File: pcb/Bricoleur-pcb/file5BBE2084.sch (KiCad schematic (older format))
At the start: 4 parts

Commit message: Schematics and footprints almost done
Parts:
- added C14, C15, C16: 1N, Capacitor_SMD:C_0402_1005Metric, symbol Device:C
- added D1, D2, D3: LED, LED_SMD:LED_0201_0603Metric, symbol Device:LED
- added R10, R9: 3K, Capacitor_SMD:C_0402_1005Metric, symbol Device:R
- added R11, R12, R13: 100R, Resistor_SMD:R_0402_1005Metric, symbol Device:R
- added R17: 100K, Resistor_SMD:R_0402_1005Metric, symbol Device:R
- added R5, R6, R7: 1M, Resistor_SMD:R_0402_1005Metric, symbol Device:R
- added R8: 3K, Resistor_SMD:R_0402_1005Metric, symbol Device:R
- added SW3, SW4, SW5: SW_Push, Bricoleur-custom:SWITCH_WURTH_4301182043816, symbol Switch:SW_Push
- added U10: VESD05A8A-HNH, Bricoleur-custom:VESD05A8A-HNH, symbol Bricoleur-pcb-cache:VESD05A8A-HNH
- J2: renamed from J?; footprint (none) -> Connector_PinHeader_2.54mm:PinHeader_2x10_P2.54mm_Vertical
- R14, R15: renamed from R?; footprint (none) -> Resistor_SMD:R_0402_1005Metric
- R16: renamed from R?; value R -> 10K; footprint (none) -> Resistor_SMD:R_0402_1005Metric
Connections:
- net labels added: DBG_LED_1, DBG_LED_2, DBG_LED_3, DBG_PB_1, DBG_PB_2, DBG_PB_3
- net labels removed: DH_RTCK
- wire segments 24 -> 90
- no-connect marks 0 -> 1

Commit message: Start of layout work + minor tweaks
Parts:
- J2: footprint Connector_PinHeader_2.54mm:PinHeader_2x10_P2.54mm_Vertical -> Connector_IDC:IDC-Header_2x10_P2.54mm_Vertical
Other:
- note removed: "UNFINISHED\n"
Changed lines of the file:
@@
 F 0 "J2" H 9100 2717 50  0000 C CNN
 F 1 "Conn_02x10_Odd_Even" H 9100 2626 50  0000 C CNN
-F 2 "Connector_PinHeader_2.54mm:PinHeader_2x10_P2.54mm_Vertical" H 9050 2100 50  0001 C CNN
+F 2 "Connector_IDC:IDC-Header_2x10_P2.54mm_Vertical" H 9050 2100 50  0001 C CNN
 F 3 "~" H 9050 2100 50  0001 C CNN
 	1    9050 2100
@@
 Text GLabel 9950 2500 3    50   Input ~ 0
 DEBUG_EXT_CABLE_ATTACH
-Text Notes 10400 2150 1    50   ~ 0
-UNFINISHED\n
 $Comp
 L Device:LED D1

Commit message: Finished camera connection, started on MC. Changed debug protection diodes sharing pattern to match debug connector.
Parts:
- U10: symbol Bricoleur-pcb-cache:VESD05A8A-HNH -> Bricoleur-pcb-rescue:VESD05A8A-HNH-Bricoleur-pcb-cache
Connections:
- wire segments 90 -> 84
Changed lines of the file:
@@
 Text GLabel 9500 2900 3    50   Input ~ 0
 GND
-Wire Wire Line
-	9350 2500 9850 2500
 Text GLabel 9950 1650 1    50   Input ~ 0
 PYNQ_3V3
@@
 Wire Wire Line
 	4700 1550 5200 1550
-Connection ~ 5200 1550
-Wire Wire Line
-	5200 1550 5500 1550
-Connection ~ 5500 1550
 Wire Wire Line
 	5500 1550 5750 1550
@@
 Wire Wire Line
 	4700 1800 4700 1750
-Connection ~ 5200 1800
 Wire Wire Line
 	5200 1800 4700 1800
-Connection ~ 5500 1800
-Wire Wire Line
-	5500 1800 5200 1800
 Wire Wire Line
 	5750 2100 5500 2100
 Wire Wire Line
 	4700 2100 4700 2050
-Connection ~ 5200 2100
 Wire Wire Line
 	5200 2100 4700 2100
-Connection ~ 5500 2100
-Wire Wire Line
-	5500 2100 5200 2100
 Wire Wire Line
 	6050 1550 6200 1550
@@
 	5150 4550 5150 4450
 $Comp
-L Bricoleur-pcb-cache:VESD05A8A-HNH U10
+L Bricoleur-pcb-rescue:VESD05A8A-HNH-Bricoleur-pcb-cache U10
 U 1 1 5BA605D7
 P 8300 1550
@@
 $EndComp
 Wire Wire Line
-	8750 1300 8750 1400
-Wire Wire Line
-	8750 1400 9850 1400
-Wire Wire Line
-	9850 1400 9850 2500
-Connection ~ 9850 2500
-Wire Wire Line
-	9850 2500 9950 2500
-Wire Wire Line
-	8850 1700 8650 1700
-Wire Wire Line
-	8850 1800 8550 1800
-Wire Wire Line
-	8850 1900 8450 1900
-Wire Wire Line
-	8850 2000 8350 2000
-Wire Wire Line
-	8850 2100 8250 2100
-Wire Wire Line
-	8850 2400 8050 2400
-Wire Wire Line
-	8650 1300 8650 1700
-Connection ~ 8650 1700
-Wire Wire Line
-	8650 1700 7850 1700
-Wire Wire Line
-	8550 1300 8550 1800
-Connection ~ 8550 1800
-Wire Wire Line
-	8550 1800 7850 1800
-Wire Wire Line
-	8450 1300 8450 1900
-Connection ~ 8450 1900
-Wire Wire Line
-	8450 1900 7850 1900
-Wire Wire Line
-	8350 1300 8350 2000
-Connection ~ 8350 2000
-Wire Wire Line
-	8350 2000 7850 2000
-Wire Wire Line
-	8250 1300 8250 2100
-Connection ~ 8250 2100
-Wire Wire Line
-	8250 2100 7850 2100
-Wire Wire Line
 	7100 2200 8850 2200
-Wire Wire Line
-	7850 2300 8150 2300
-Wire Wire Line
-	8150 1300 8150 2300
-Connection ~ 8150 2300
-Wire Wire Line
-	8150 2300 8850 2300
-Wire Wire Line
-	8050 1300 8050 2400
-Connection ~ 8050 2400
-Wire Wire Line
-	8050 2400 7850 2400
 Text GLabel 8050 750  2    50   Input ~ 0
 GND
@@
 VMCU
 NoConn ~ 9350 1700
+Wire Wire Line
+	9350 2500 9950 2500
+Text GLabel 8050 2450 3    50   Input ~ 0
+DEBUG_EXT_CABLE_ATTACH
+Wire Wire Line
+	7850 2100 8350 2100
+Wire Wire Line
+	7850 2300 8250 2300
+Wire Wire Line
+	7850 2400 8150 2400
+Wire Wire Line
+	7850 2000 8750 2000
+Wire Wire Line
+	7850 1900 8650 1900
+Wire Wire Line
+	7850 1700 8450 1700
+Wire Wire Line
+	7850 1800 8550 1800
+Wire Wire Line
+	8450 1300 8450 1700
+Connection ~ 8450 1700
+Wire Wire Line
+	8450 1700 8850 1700
+Wire Wire Line
+	8550 1300 8550 1800
+Connection ~ 8550 1800
+Wire Wire Line
+	8550 1800 8850 1800
+Wire Wire Line
+	8650 1300 8650 1900
+Connection ~ 8650 1900
+Wire Wire Line
+	8650 1900 8850 1900
+Wire Wire Line
+	8750 1300 8750 2000
+Connection ~ 8750 2000
+Wire Wire Line
+	8750 2000 8850 2000
+Wire Wire Line
+	8350 1300 8350 2100
+Connection ~ 8350 2100
+Wire Wire Line
+	8350 2100 8850 2100
+Wire Wire Line
+	8250 1300 8250 2300
+Connection ~ 8250 2300
+Wire Wire Line
+	8250 2300 8850 2300
+Wire Wire Line
+	8150 1300 8150 2400
+Connection ~ 8150 2400
+Wire Wire Line
+	8150 2400 8850 2400
+Wire Wire Line
+	8050 1300 8050 2450
 $EndSCHEMATC

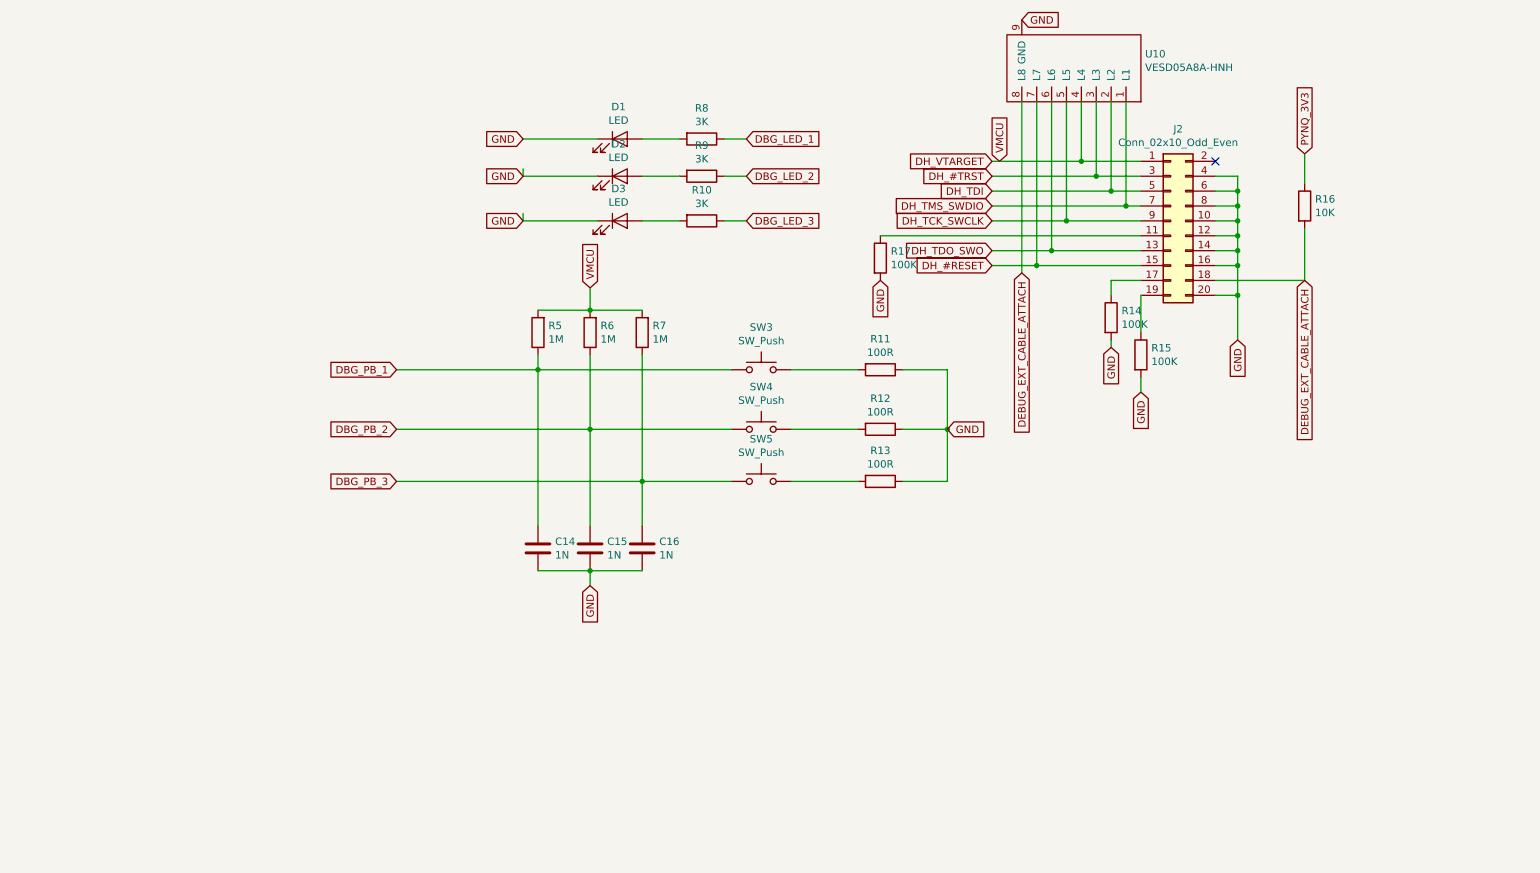
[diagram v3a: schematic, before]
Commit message: More ESD protection, USART output, more footprints
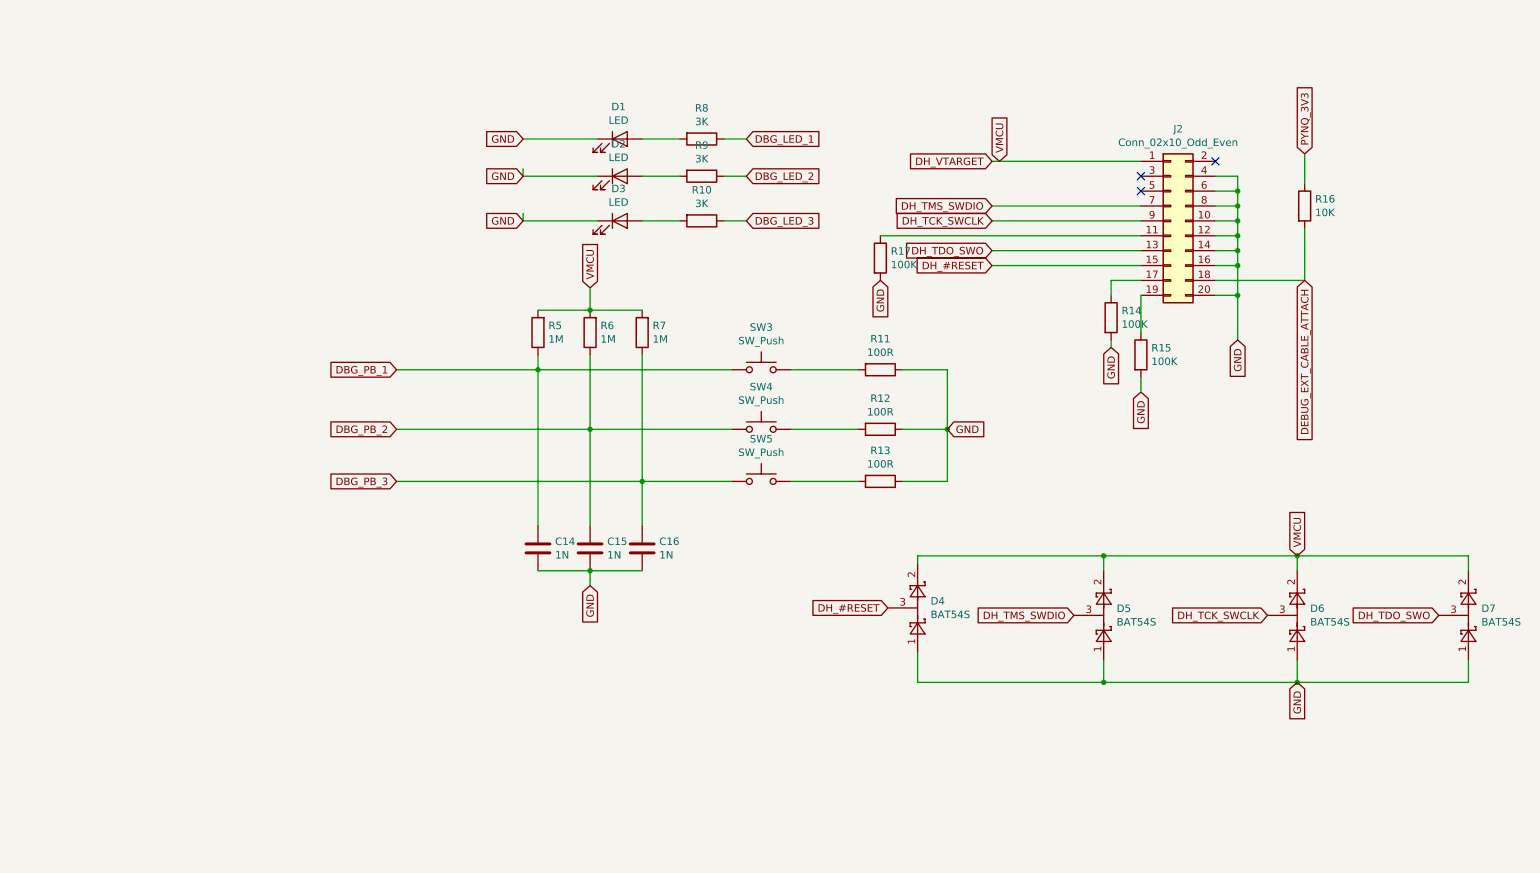
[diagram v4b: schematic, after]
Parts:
- removed U10: VESD05A8A-HNH, Bricoleur-custom:VESD05A8A-HNH, symbol Bricoleur-pcb-rescue:VESD05A8A-HNH-Bricoleur-pcb-cache
- added D4, D5, D6, D7: BAT54S, Package_TO_SOT_SMD:SOT-23, symbol Diode:BAT54S
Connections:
- net DH_#RESET: now also D4.3
- net DH_TCK_SWCLK: now also D6.3
- net DH_TDO_SWO: now also D7.3
- net DH_TMS_SWDIO: now also D5.3
- net DH_VTARGET: now also D4.2, D5.2, D6.2, D7.2
- net GND: now also D4.1, D5.1, D6.1, D7.1
- net DH_#TRST: no longer names the net of J2.3 (Pin_3)
- net DH_TDI: no longer names the net of J2.5 (Pin_5)
- no-connect marks 1 -> 3
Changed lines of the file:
@@
 $Descr A4 11693 8268
 encoding utf-8
-Sheet 2 3
+Sheet 2 18
 Title ""
 Date ""
@@
 Text GLabel 7850 1700 0    50   Input ~ 0
 DH_VTARGET
-Text GLabel 7850 1800 0    50   Input ~ 0
-DH_#TRST
-Text GLabel 7850 1900 0    50   Input ~ 0
-DH_TDI
 Text GLabel 7850 2000 0    50   Input ~ 0
 DH_TMS_SWDIO
@@
 DBG_PB_3
 Wire Wire Line
-	3850 3100 4800 3100
-Wire Wire Line
-	6100 3500 5150 3500
-Wire Wire Line
-	6100 3850 5500 3850
-Wire Wire Line
 	5150 2550 5150 2700
-Wire Wire Line
-	5500 2700 5150 2700
-Connection ~ 5150 2700
-Wire Wire Line
-	5150 2700 4800 2700
-Wire Wire Line
-	4800 3000 4800 3100
-Connection ~ 4800 3100
-Wire Wire Line
-	4800 3100 6100 3100
-Wire Wire Line
-	4800 3100 4800 4150
 Wire Wire Line
 	5150 3000 5150 3500
 Connection ~ 5150 3500
 Wire Wire Line
-	5150 3500 3850 3500
-Wire Wire Line
 	5150 3500 5150 4150
 Wire Wire Line
@@
 Connection ~ 5500 3850
 Wire Wire Line
-	5500 3850 3850 3850
-Wire Wire Line
 	5500 3850 5500 4150
 Wire Wire Line
@@
 GND
 Wire Wire Line
-	5500 4450 5150 4450
-Connection ~ 5150 4450
-Wire Wire Line
-	5150 4450 4800 4450
-Wire Wire Line
 	5150 4550 5150 4450
-$Comp
-L Bricoleur-pcb-rescue:VESD05A8A-HNH-Bricoleur-pcb-cache U10
-U 1 1 5BA605D7
-P 8300 1550
-F 0 "U10" H 7722 979 50  0000 R CNN
-F 1 "VESD05A8A-HNH" H 7722 1070 50  0000 R CNN
-F 2 "Bricoleur-custom:VESD05A8A-HNH" H 8300 1550 50  0001 C CNN
-F 3 "" H 8300 1550 50  0001 C CNN
-	1    8300 1550
-	-1   0    0    1
-$EndComp
 Wire Wire Line
 	7100 2200 8850 2200
-Text GLabel 8050 750  2    50   Input ~ 0
-GND
 $Comp
 L Device:R R17
@@
 Wire Wire Line
 	9350 2500 9950 2500
-Text GLabel 8050 2450 3    50   Input ~ 0
-DEBUG_EXT_CABLE_ATTACH
-Wire Wire Line
-	7850 2100 8350 2100
-Wire Wire Line
-	7850 2300 8250 2300
-Wire Wire Line
-	7850 2400 8150 2400
-Wire Wire Line
-	7850 2000 8750 2000
-Wire Wire Line
-	7850 1900 8650 1900
-Wire Wire Line
-	7850 1700 8450 1700
-Wire Wire Line
-	7850 1800 8550 1800
-Wire Wire Line
-	8450 1300 8450 1700
-Connection ~ 8450 1700
-Wire Wire Line
-	8450 1700 8850 1700
-Wire Wire Line
-	8550 1300 8550 1800
-Connection ~ 8550 1800
-Wire Wire Line
-	8550 1800 8850 1800
-Wire Wire Line
-	8650 1300 8650 1900
-Connection ~ 8650 1900
-Wire Wire Line
-	8650 1900 8850 1900
-Wire Wire Line
-	8750 1300 8750 2000
-Connection ~ 8750 2000
-Wire Wire Line
-	8750 2000 8850 2000
-Wire Wire Line
-	8350 1300 8350 2100
-Connection ~ 8350 2100
-Wire Wire Line
-	8350 2100 8850 2100
-Wire Wire Line
-	8250 1300 8250 2300
-Connection ~ 8250 2300
-Wire Wire Line
-	8250 2300 8850 2300
-Wire Wire Line
-	8150 1300 8150 2400
-Connection ~ 8150 2400
-Wire Wire Line
-	8150 2400 8850 2400
-Wire Wire Line
-	8050 1300 8050 2450
+Wire Wire Line
+	3850 3100 4800 3100
+Wire Wire Line
+	4800 3100 4800 4150
+Wire Wire Line
+	4800 3000 4800 3100
+Connection ~ 4800 3100
+Wire Wire Line
+	4800 3100 6100 3100
+Wire Wire Line
+	6100 3500 5150 3500
+Wire Wire Line
+	6100 3850 5500 3850
+Connection ~ 5150 2700
+Wire Wire Line
+	5500 2700 5150 2700
+Wire Wire Line
+	5150 2700 4800 2700
+Connection ~ 5150 4450
+Wire Wire Line
+	5500 4450 5150 4450
+Wire Wire Line
+	5150 4450 4800 4450
+Wire Wire Line
+	5150 3500 3850 3500
+Wire Wire Line
+	5500 3850 3850 3850
+NoConn ~ 8850 1800
+NoConn ~ 8850 1900
+$Comp
+L Diode:BAT54S D5
+U 1 1 5BB434F5
+P 8600 4750
+F 0 "D5" V 8646 4837 50  0000 L CNN
+F 1 "BAT54S" V 8555 4837 50  0000 L CNN
+F 2 "Package_TO_SOT_SMD:SOT-23" H 8675 4875 50  0001 L CNN
+F 3 "https://www.diodes.com/assets/Datasheets/ds11005.pdf" H 8480 4750 50  0001 C CNN
+	1    8600 4750
+	0    1    -1   0
+$EndComp
+Wire Wire Line
+	7850 2400 8850 2400
+Wire Wire Line
+	7850 2300 8850 2300
+Wire Wire Line
+	7850 2100 8850 2100
+Wire Wire Line
+	7850 1700 8850 1700
+Wire Wire Line
+	7850 2000 8850 2000
+Text GLabel 8400 4750 0    50   Input ~ 0
+DH_TMS_SWDIO
+Text GLabel 9700 4750 0    50   Input ~ 0
+DH_TCK_SWCLK
+$Comp
+L Diode:BAT54S D6
+U 1 1 5BB4DE32
+P 9900 4750
+F 0 "D6" V 9946 4837 50  0000 L CNN
+F 1 "BAT54S" V 9855 4837 50  0000 L CNN
+F 2 "Package_TO_SOT_SMD:SOT-23" H 9975 4875 50  0001 L CNN
+F 3 "https://www.diodes.com/assets/Datasheets/ds11005.pdf" H 9780 4750 50  0001 C CNN
+	1    9900 4750
+	0    1    -1   0
+$EndComp
+Text GLabel 10850 4750 0    50   Input ~ 0
+DH_TDO_SWO
+$Comp
+L Diode:BAT54S D7
+U 1 1 5BB4DEDC
+P 11050 4750
+F 0 "D7" V 11096 4837 50  0000 L CNN
+F 1 "BAT54S" V 11005 4837 50  0000 L CNN
+F 2 "Package_TO_SOT_SMD:SOT-23" H 11125 4875 50  0001 L CNN
+F 3 "https://www.diodes.com/assets/Datasheets/ds11005.pdf" H 10930 4750 50  0001 C CNN
+	1    11050 4750
+	0    1    -1   0
+$EndComp
+Wire Wire Line
+	11050 5050 11050 5200
+Wire Wire Line
+	11050 5200 9900 5200
+Wire Wire Line
+	8600 5200 8600 5050
+Wire Wire Line
+	9900 5050 9900 5200
+Connection ~ 9900 5200
+Wire Wire Line
+	9900 5200 8600 5200
+Wire Wire Line
+	11050 4450 11050 4350
+Wire Wire Line
+	11050 4350 9900 4350
+Wire Wire Line
+	8600 4350 8600 4450
+Wire Wire Line
+	9900 4450 9900 4350
+Connection ~ 9900 4350
+Wire Wire Line
+	9900 4350 8600 4350
+Text GLabel 9900 5200 3    50   Input ~ 0
+GND
+Text GLabel 9900 4350 1    50   Input ~ 0
+VMCU
+Text GLabel 7150 4700 0    50   Input ~ 0
+DH_#RESET
+$Comp
+L Diode:BAT54S D4
+U 1 1 5BB621C0
+P 7350 4700
+F 0 "D4" V 7396 4787 50  0000 L CNN
+F 1 "BAT54S" V 7305 4787 50  0000 L CNN
+F 2 "Package_TO_SOT_SMD:SOT-23" H 7425 4825 50  0001 L CNN
+F 3 "https://www.diodes.com/assets/Datasheets/ds11005.pdf" H 7230 4700 50  0001 C CNN
+	1    7350 4700
+	0    1    -1   0
+$EndComp
+Wire Wire Line
+	8600 4350 7350 4350
+Wire Wire Line
+	7350 4350 7350 4400
+Connection ~ 8600 4350
+Wire Wire Line
+	8600 5200 7350 5200
+Wire Wire Line
+	7350 5200 7350 5000
+Connection ~ 8600 5200
 $EndSCHEMATC

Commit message: PCB…
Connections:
- net DH_VTARGET renamed VMCU
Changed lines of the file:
@@
 Text GLabel 8650 2950 3    50   Input ~ 0
 GND
-Text GLabel 7850 1700 0    50   Input ~ 0
-DH_VTARGET
 Text GLabel 7850 2000 0    50   Input ~ 0
 DH_TMS_SWDIO
@@
 Text GLabel 7100 2500 3    50   Input ~ 0
 GND
-Text GLabel 7900 1700 1    50   Input ~ 0
+Text GLabel 7900 1600 1    50   Input ~ 0
 VMCU
 NoConn ~ 9350 1700
@@
 	7850 2100 8850 2100
 Wire Wire Line
-	7850 1700 8850 1700
-Wire Wire Line
 	7850 2000 8850 2000
 Text GLabel 8400 4750 0    50   Input ~ 0
@@
 	7350 5200 7350 5000
 Connection ~ 8600 5200
+Wire Wire Line
+	7900 1700 7900 1600
+Wire Wire Line
+	7900 1700 8850 1700
 $EndSCHEMATC

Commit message: Overwrite
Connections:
- net PYNQ_3V3 is gone; now on net VMCU: R16.1
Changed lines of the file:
@@
 GND
 Text GLabel 9950 1650 1    50   Input ~ 0
-PYNQ_3V3
+VMCU
 $Comp
 L Device:R R16
